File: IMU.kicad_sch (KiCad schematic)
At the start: 4 parts

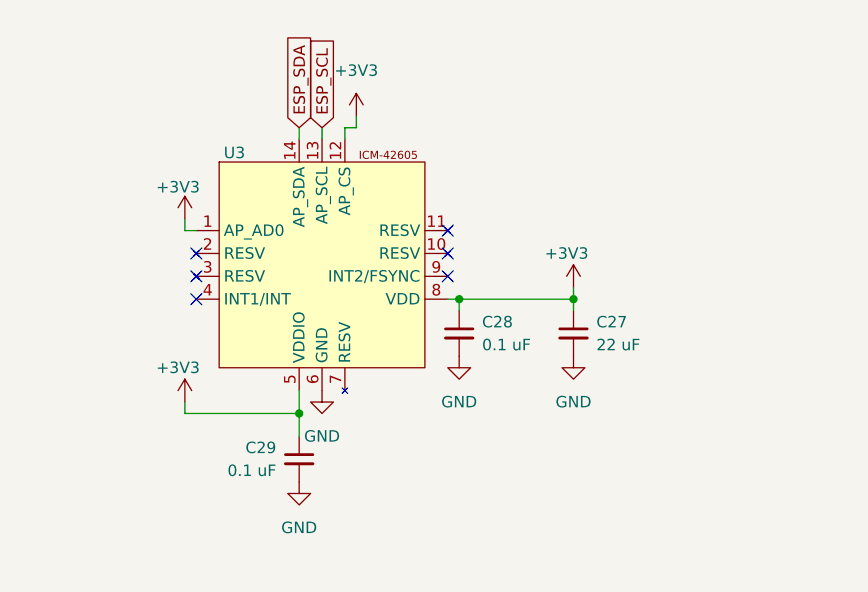
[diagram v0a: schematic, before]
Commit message: Wired barometers and GPS up, added misc LEDs, tidy-up
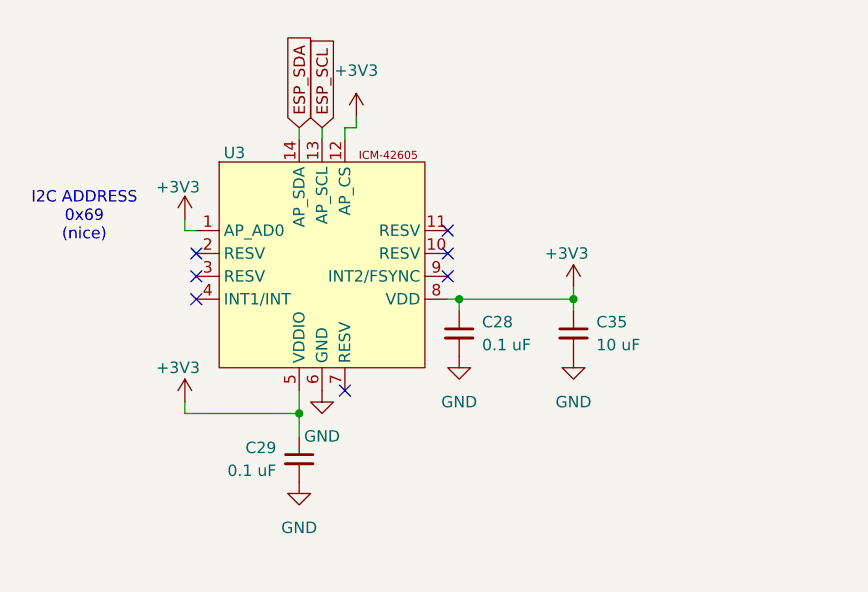
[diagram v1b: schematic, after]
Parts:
- removed C27: 22 uF, symbol Device:C_Small
- added C35: 10 uF, symbol Device:C_Small
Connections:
- net +3V3: now also C35.1
- net GND: now also C35.2
- no-connect marks 6 -> 7
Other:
- note added: "I2C ADDRESS 0x69 (nice)"
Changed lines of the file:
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@@
 		(company "Süalp K.")
+	)
+	(text "I2C ADDRESS\n0x69\n(nice)"
+		(exclude_from_sim no)
+		(at 98.044 81.026 0)
+		(effects
+			(font
+				(size 1.27 1.27)
+			)
+		)
 	)
 	(junction
@@
 	(no_connect
 		(at 138.43 87.63)
+	)
+	(no_connect
+		(at 127 100.33)
 	)
 	(no_connect
@@
 	)
 	(symbol
-		(lib_id "Device:C_Small")
-		(at 152.4 93.98 0)
-		(mirror y)
-		(unit 1)
-		(exclude_from_sim no)
-		(in_bom yes)
-		(on_board yes)
-		(dnp no)
-		(property "Reference" "C27"
-			(at 154.94 92.7162 0)
-			(effects
-				(font
-					(size 1.27 1.27)
-				)
-				(justify right)
-			)
-		)
-		(property "Value" "22 uF"
-			(at 154.94 95.2562 0)
-			(effects
-				(font
-					(size 1.27 1.27)
-				)
-				(justify right)
-			)
-		)
-		(property "Footprint" ""
-			(at 152.4 93.98 0)
-			(effects
-				(font
-					(size 1.27 1.27)
-				)
-				(hide yes)
-			)
-		)
-		(property "Datasheet" "~"
-			(at 152.4 93.98 0)
-			(effects
-				(font
-					(size 1.27 1.27)
-				)
-				(hide yes)
-			)
-		)
-		(property "Description" "Unpolarized capacitor, small symbol"
-			(at 152.4 93.98 0)
-			(effects
-				(font
-					(size 1.27 1.27)
-				)
-				(hide yes)
-			)
-		)
-		(pin "1"
-		)
-		(pin "2"
-		)
-		(instances
-			(project "valkyriev3"
-				(path "/d24fd15c-a242-4d26-9876-7755ca0d378c/0956f2c5-d311-4a6e-b6b6-3effe6c70a2d"
-					(reference "C27")
-					(unit 1)
-				)
-			)
-		)
-	)
-	(symbol
 		(lib_id "power:GND")
 		(at 124.46 100.33 0)
@@
 					(unit 1)
 				)
+			)
+		)
+	)
+	(symbol
+		(lib_id "Device:C_Small")
+		(at 152.4 93.98 0)
+		(mirror y)
+		(unit 1)
+		(exclude_from_sim no)
+		(in_bom yes)
+		(on_board yes)
+		(dnp no)
+		(property "Reference" "C35"
+			(at 154.94 92.7162 0)
+			(effects
+				(font
+					(size 1.27 1.27)
+				)
+				(justify right)
+			)
+		)
+		(property "Value" "10 uF"
+			(at 154.94 95.2562 0)
+			(effects
+				(font
+					(size 1.27 1.27)
+				)
+				(justify right)
+			)
+		)
+		(property "Footprint" ""
+			(at 152.4 93.98 0)
+			(effects
+				(font
+					(size 1.27 1.27)
+				)
+				(hide yes)
+			)
+		)
+		(property "Datasheet" "~"
+			(at 152.4 93.98 0)
+			(effects
+				(font
+					(size 1.27 1.27)
+				)
+				(hide yes)
+			)
+		)
+		(property "Description" "Unpolarized capacitor, small symbol"
+			(at 152.4 93.98 0)
+			(effects
+				(font
+					(size 1.27 1.27)
+				)
+				(hide yes)
+			)
+		)
+		(pin "1"
+		)
+		(pin "2"
+		)
+		(instances
+			(project "valkyriev3"
+				(path "/d24fd15c-a242-4d26-9876-7755ca0d378c/0956f2c5-d311-4a6e-b6b6-3effe6c70a2d"
+					(reference "C35")
+					(unit 1)
+				)

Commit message: preliminary schematic wired, all footprints assigned, all laid out in PCB editor.
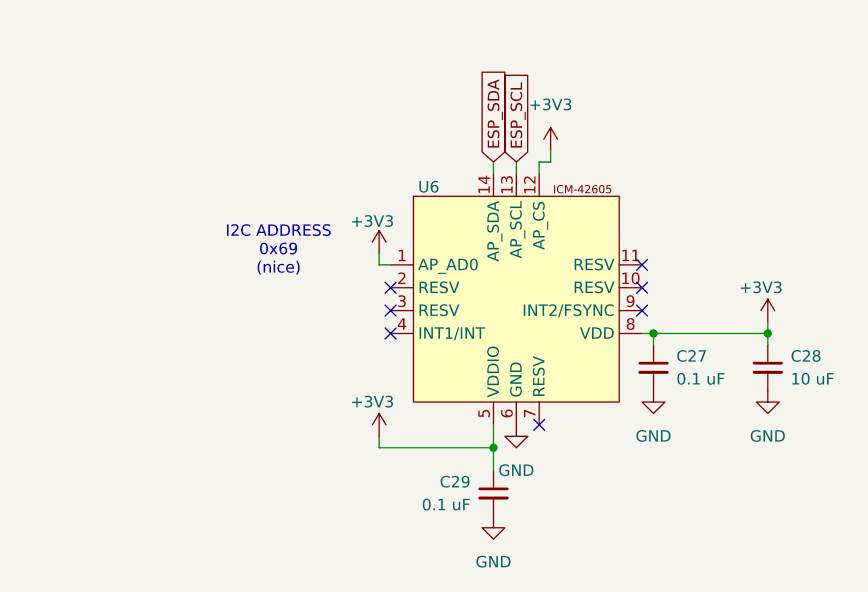
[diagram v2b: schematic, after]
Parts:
- C28: renamed from C35; footprint (none) -> Capacitor_SMD:C_0603_1608Metric
- renumbered C28 to C27, U3 to U6
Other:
- moved on the sheet: C27, C28, C29, U6

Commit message: reassigned some footprints, preliminary PCB layout
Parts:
- C27, C29: footprint Capacitor_SMD:C_0805_2012Metric -> Capacitor_SMD:C_0603_1608Metric
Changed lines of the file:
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@@
 			)
 		)
-		(property "Footprint" "Capacitor_SMD:C_0805_2012Metric"
+		(property "Footprint" "Capacitor_SMD:C_0603_1608Metric"
 			(at 143.51 111.76 0)
 			(effects
@@
 			)
 		)
-		(property "Footprint" "Capacitor_SMD:C_0805_2012Metric"
+		(property "Footprint" "Capacitor_SMD:C_0603_1608Metric"
 			(at 161.29 97.79 0)
 			(effects

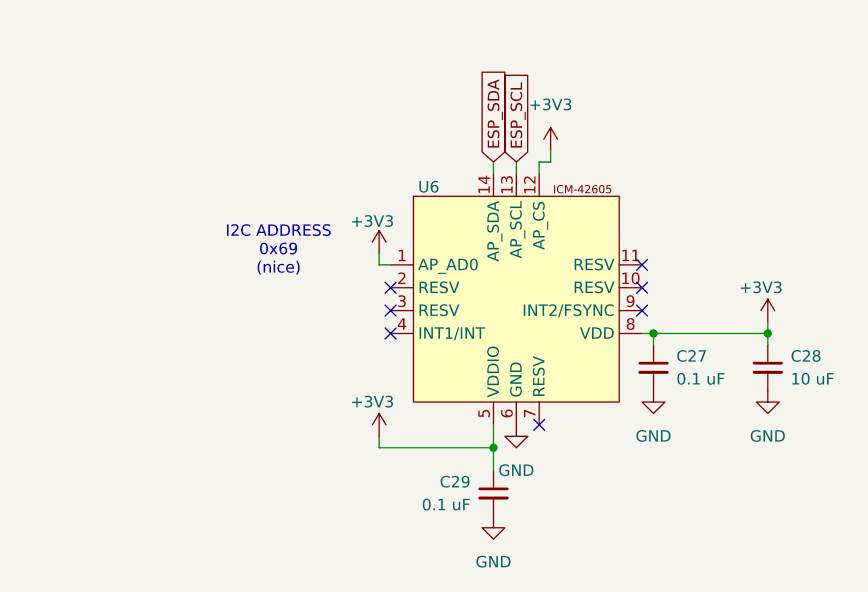
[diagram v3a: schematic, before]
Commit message: connected IMU pins 7 and 9 to GND instead of NC
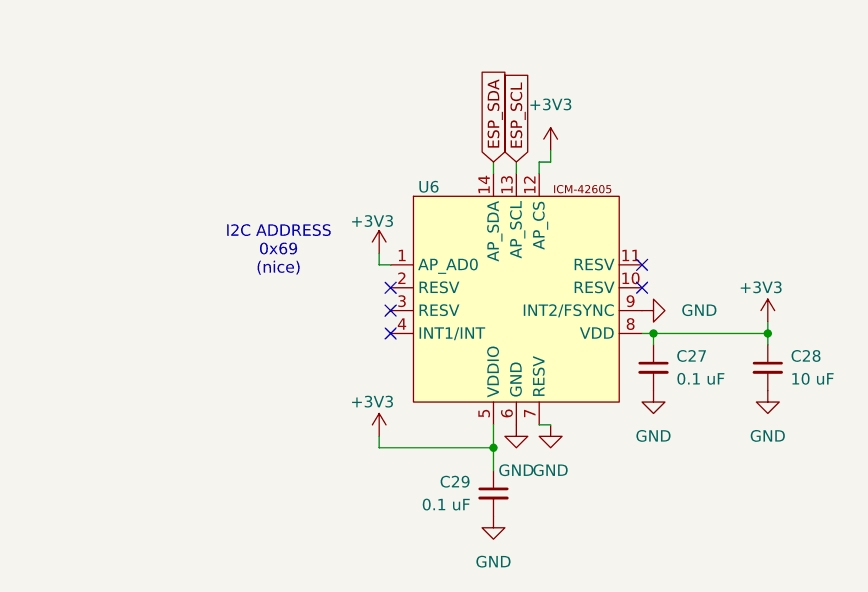
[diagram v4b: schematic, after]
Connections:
- net GND: now also U6.7 (RESV), U6.9 (INT2/FSYNC)
- no-connect marks 7 -> 5
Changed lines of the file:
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@@
-	)
-	(no_connect
-		(at 160.02 91.44)
-	)
-	(no_connect
-		(at 148.59 104.14)
 	)
 	(no_connect
@@
 		(pts
 			(xy 130.81 105.41) (xy 130.81 106.68)
+		)
+		(stroke
+			(width 0)
+			(type default)
+		)
+	)
+	(wire
+		(pts
+			(xy 149.86 104.14) (xy 148.59 104.14)
 		)
 		(stroke
@@
 	)
 	(symbol
+		(lib_id "power:GND")
+		(at 160.02 91.44 90)
+		(unit 1)
+		(exclude_from_sim no)
+		(in_bom yes)
+		(on_board yes)
+		(dnp no)
+		(fields_autoplaced yes)
+		(property "Reference" "#PWR0121"
+			(at 166.37 91.44 0)
+			(effects
+				(font
+					(size 1.27 1.27)
+				)
+				(hide yes)
+			)
+		)
+		(property "Value" "GND"
+			(at 164.3882 91.4399 90)
+			(effects
+				(font
+					(size 1.27 1.27)
+				)
+				(justify right)
+			)
+		)
+		(property "Footprint" ""
+			(at 160.02 91.44 0)
+			(effects
+				(font
+					(size 1.27 1.27)
+				)
+				(hide yes)
+			)
+		)
+		(property "Datasheet" ""
+			(at 160.02 91.44 0)
+			(effects
+				(font
+					(size 1.27 1.27)
+				)
+				(hide yes)
+			)
+		)
+		(property "Description" "Power symbol creates a global label with name \"GND\" , ground"
+			(at 160.02 91.44 0)
+			(effects
+				(font
+					(size 1.27 1.27)
+				)
+				(hide yes)
+			)
+		)
+		(pin "1"
+		)
+		(instances
+			(project "valkyriev3"
+				(path "/d24fd15c-a242-4d26-9876-7755ca0d378c/0956f2c5-d311-4a6e-b6b6-3effe6c70a2d"
+					(reference "#PWR0121")
+					(unit 1)
+				)
+			)
+		)
+	)
+	(symbol
 		(lib_id "power:+3V3")
 		(at 130.81 105.41 0)
@@
 					(unit 1)
 				)
+			)
+		)
+	)
+	(symbol
+		(lib_id "power:GND")
+		(at 149.86 104.14 0)
+		(unit 1)
+		(exclude_from_sim no)
+		(in_bom yes)
+		(on_board yes)
+		(dnp no)
+		(fields_autoplaced yes)
+		(property "Reference" "#PWR0120"
+			(at 149.86 110.49 0)
+			(effects
+				(font
+					(size 1.27 1.27)
+				)
+				(hide yes)
+			)
+		)
+		(property "Value" "GND"
+			(at 149.86 109.22 0)
+			(effects
+				(font
+					(size 1.27 1.27)
+				)
+			)
+		)
+		(property "Footprint" ""
+			(at 149.86 104.14 0)
+			(effects
+				(font
+					(size 1.27 1.27)
+				)
+				(hide yes)
+			)
+		)
+		(property "Datasheet" ""
+			(at 149.86 104.14 0)
+			(effects
+				(font
+					(size 1.27 1.27)
+				)
+				(hide yes)
+			)
+		)
+		(property "Description" "Power symbol creates a global label with name \"GND\" , ground"
+			(at 149.86 104.14 0)
+			(effects
+				(font
+					(size 1.27 1.27)
+				)
+				(hide yes)
+			)
+		)
+		(pin "1"
+		)
+		(instances
+			(project "valkyriev3"
+				(path "/d24fd15c-a242-4d26-9876-7755ca0d378c/0956f2c5-d311-4a6e-b6b6-3effe6c70a2d"
+					(reference "#PWR0120")
+					(unit 1)
+				)
